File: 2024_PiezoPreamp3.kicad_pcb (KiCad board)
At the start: 4 copper layers, 71 x 36.8 mm, 90 parts, among them J101 6.3mm stereo, J102 6.3mm stereo, J201 DC IN 5.5/2.1mm, J401 Spring Contact, U101 OPA145, U102 OPA145, U201 ZXMP3A17E6TA, U301 BC847BS,115

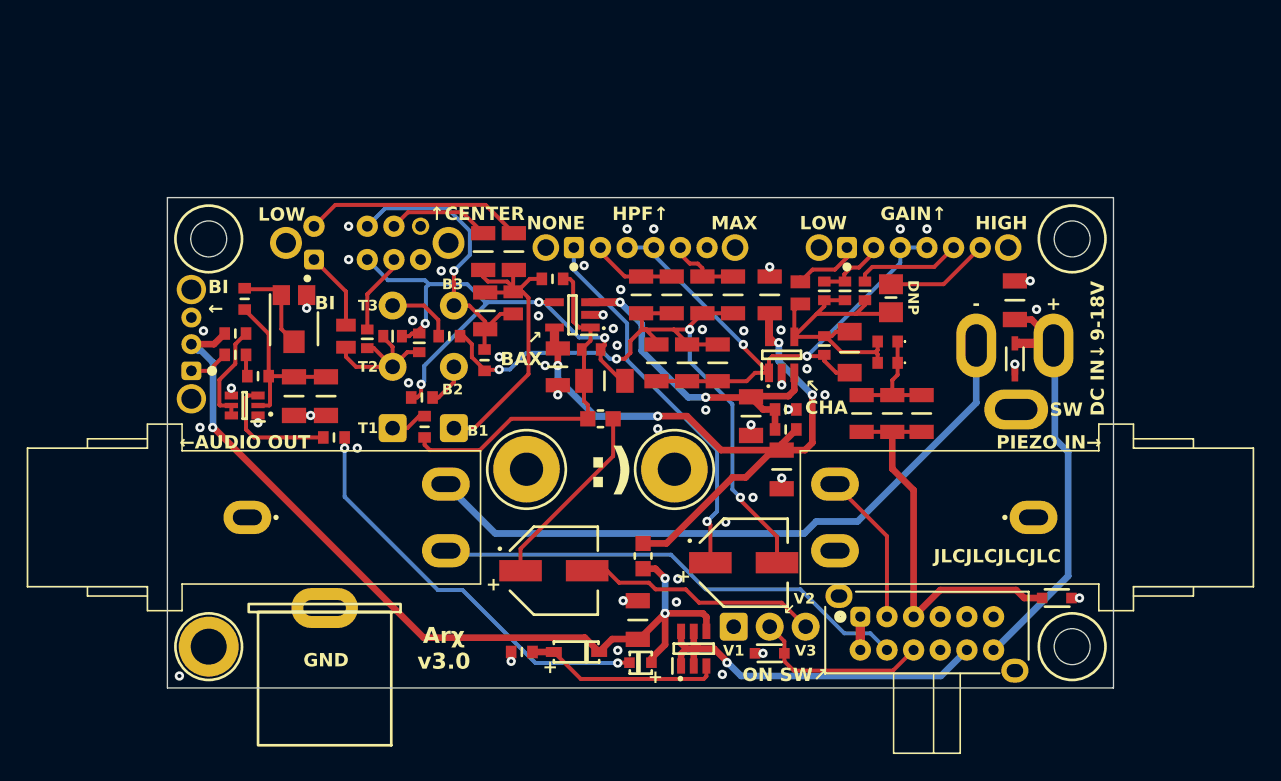
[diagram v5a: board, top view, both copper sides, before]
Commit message: PCB: moving tracks & vias so that the signals don't cross holes in gnd planes cause by signal vias
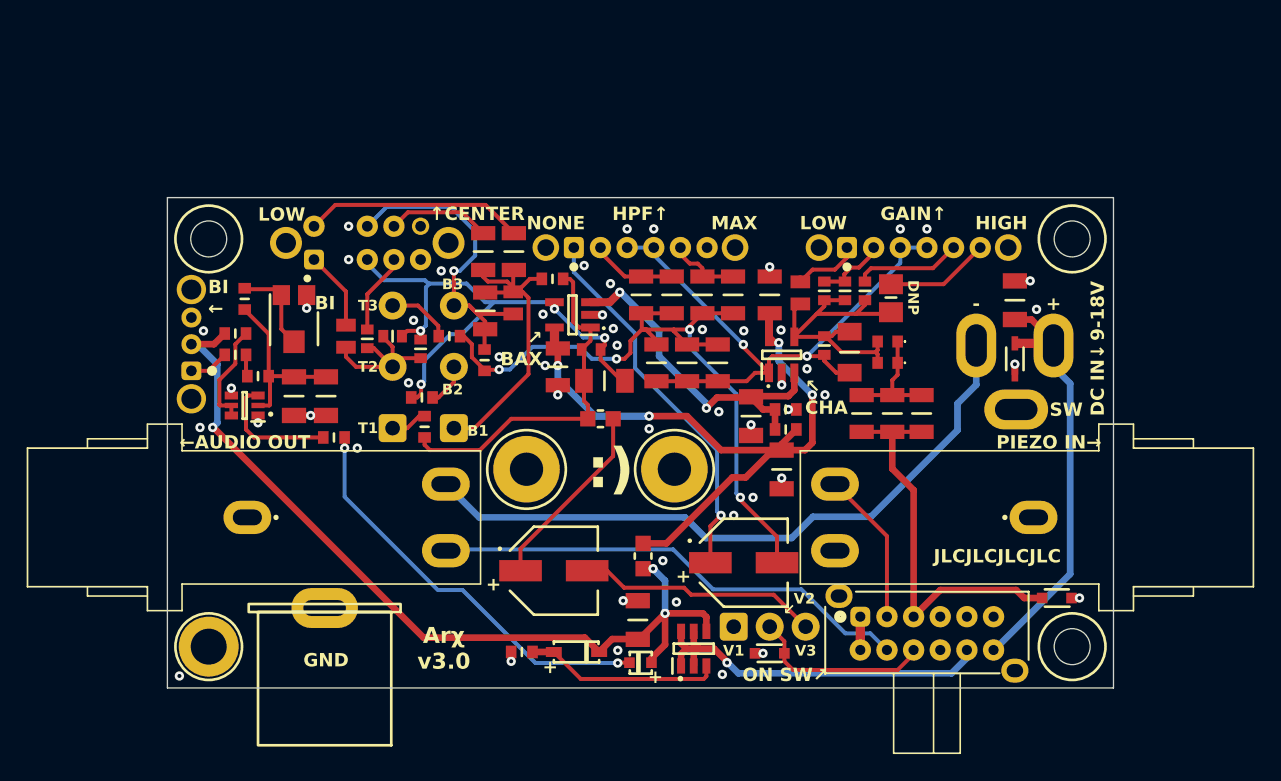
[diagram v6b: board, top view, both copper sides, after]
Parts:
- moved Ct101 0.46 mm to (133.9, 86.4)
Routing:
- net /1-ChargeAmpAndEQ/BASS_3: track 22.7 -> 24.5 mm
- net Vbias: track 24.7 -> 26.2 mm
- net DC_IN_NEG: track 49.7 -> 50.4 mm
- net VS: track 56.3 -> 55.7 mm
- net /1-ChargeAmpAndEQ/BAX_A_INV: track 41.0 -> 41.6 mm

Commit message: PCB: stitching vias
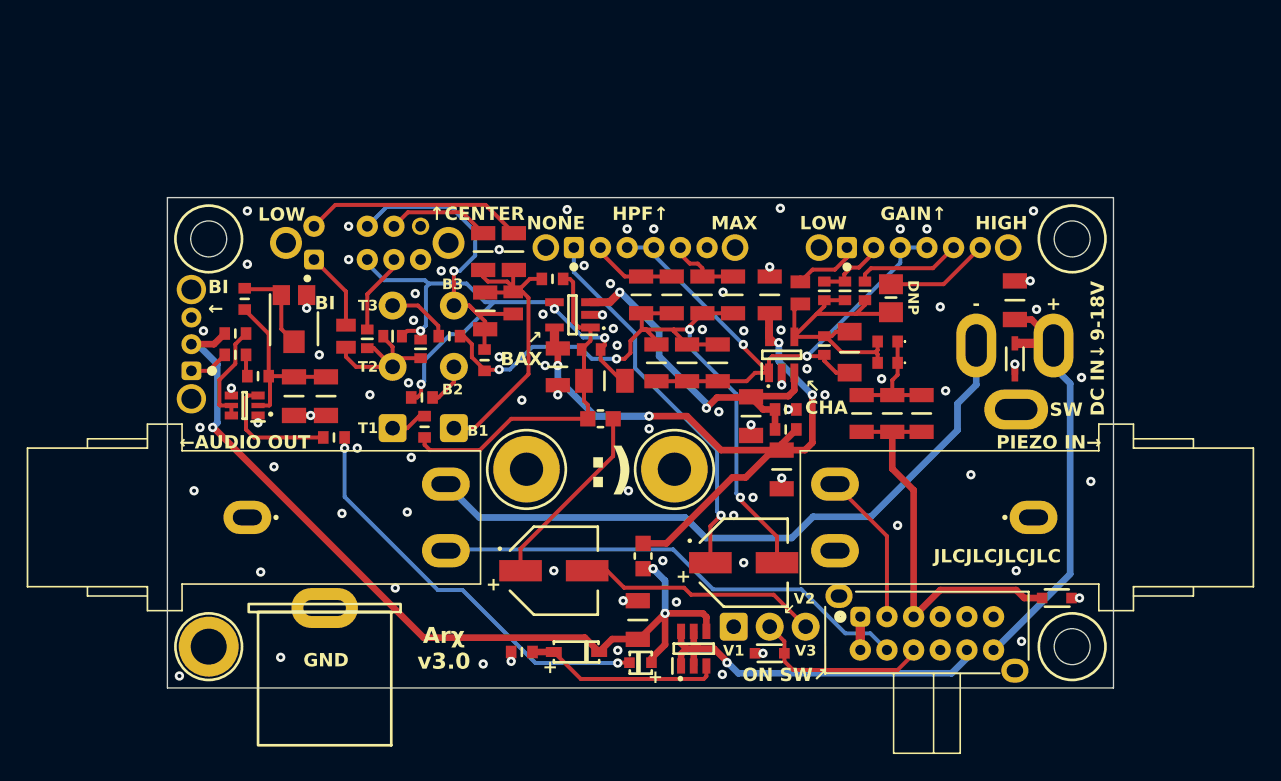
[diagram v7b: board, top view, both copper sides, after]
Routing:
- net GND: vias 51 -> 83
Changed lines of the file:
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@@
+	)
+	(via
+		(at 156.6 82.15)
+		(size 0.7)
+		(drill 0.3)
+		(layers "F.Cu" "B.Cu")
+		(net 2)
 	)
 	(via
@@
 	)
 	(via
+		(at 120.9 76.05)
+		(size 0.7)
+		(drill 0.3)
+		(layers "F.Cu" "B.Cu")
+		(net 2)
+	)
+	(via
 		(at 132.996268 88.950841)
 		(size 0.7)
@@
 	)
 	(via
+		(at 172.9 83.25)
+		(size 0.7)
+		(drill 0.3)
+		(layers "F.Cu" "B.Cu")
+		(net 2)
+	)
+	(via
 		(at 151.05 92.400003)
 		(size 0.7)
@@
 	)
 	(via
+		(at 128 98.75)
+		(size 0.7)
+		(drill 0.3)
+		(layers "F.Cu" "B.Cu")
+		(net 2)
+	)
+	(via
 		(at 159.6 109.25)
 		(size 0.7)
@@
 	)
 	(via
+		(at 143.9 103.05)
+		(size 0.7)
+		(drill 0.3)
+		(layers "F.Cu" "B.Cu")
+		(net 2)
+	)
+	(via
 		(at 152.083934 102.296651)
 		(size 0.7)
@@
 	)
 	(via
+		(at 175.2 95.85)
+		(size 0.7)
+		(drill 0.3)
+		(layers "F.Cu" "B.Cu")
+		(net 2)
+	)
+	(via
 		(at 161 89.1)
 		(size 0.7)
@@
 	)
 	(via
+		(at 133.2 94.55)
+		(size 0.7)
+		(drill 0.3)
+		(layers "F.Cu" "B.Cu")
+		(net 2)
+	)
+	(via
 		(at 148.151935 81.505632)
 		(size 0.7)
@@
 	)
 	(via
+		(at 169.7 99.65)
+		(size 0.7)
+		(drill 0.3)
+		(layers "F.Cu" "B.Cu")
+		(net 2)
+	)
+	(via
+		(at 158.15 102.45)
+		(size 0.7)
+		(drill 0.3)
+		(layers "F.Cu" "B.Cu")
+		(net 2)
+	)
+	(via
 		(at 135.449997 80.55)
 		(size 0.7)
@@
 	)
 	(via
+		(at 123.4 109.55)
+		(size 0.7)
+		(drill 0.3)
+		(layers "F.Cu" "B.Cu")
+		(net 2)
+	)
+	(via
 		(at 125.35 83.35)
 		(size 0.7)
@@
 	)
 	(via
+		(at 132 104.35)
+		(size 0.7)
+		(drill 0.3)
+		(layers "F.Cu" "B.Cu")
+		(net 2)
+	)
+	(via
 		(at 151.4 77.399997)
 		(size 0.7)
@@
 	)
 	(via
+		(at 168.5 88.65)
+		(size 0.7)
+		(drill 0.3)
+		(layers "F.Cu" "B.Cu")
+		(net 2)
+	)
+	(via
 		(at 153.1 105.4)
 		(size 0.7)
@@
 	)
 	(via
+		(at 132.9 98.65)
+		(size 0.7)
+		(drill 0.3)
+		(layers "F.Cu" "B.Cu")
+		(net 2)
+	)
+	(via
+		(at 144.9 75.95)
+		(size 0.7)
+		(drill 0.3)
+		(layers "F.Cu" "B.Cu")
+		(net 2)
+	)
+	(via
 		(at 149.1 105.3)
 		(size 0.7)
@@
 	)
 	(via
+		(at 120.9 80.05)
+		(size 0.7)
+		(drill 0.3)
+		(layers "F.Cu" "B.Cu")
+		(net 2)
+	)
+	(via
+		(at 121.9 103.15)
+		(size 0.7)
+		(drill 0.3)
+		(layers "F.Cu" "B.Cu")
+		(net 2)
+	)
+	(via
 		(at 119.7 89.35)
 		(size 0.7)
@@
 	)
 	(via
+		(at 133.5 82.25)
+		(size 0.7)
+		(drill 0.3)
+		(layers "F.Cu" "B.Cu")
+		(net 2)
+	)
+	(via
 		(at 156.284324 91.117758)
 		(size 0.7)
@@
 	)
 	(via
+		(at 184.2 96.35)
+		(size 0.7)
+		(drill 0.3)
+		(layers "F.Cu" "B.Cu")
+		(net 2)
+	)
+	(via
 		(at 121.7 91.95)
 		(size 0.7)
@@
 	)
 	(via
+		(at 179.9 76.05)
+		(size 0.7)
+		(drill 0.3)
+		(layers "F.Cu" "B.Cu")
+		(net 2)
+	)
+	(via
 		(at 178.5 87.55)
 		(size 0.7)
@@
 	)
 	(via
+		(at 138.6 110.05)
+		(size 0.7)
+		(drill 0.3)
+		(layers "F.Cu" "B.Cu")
+		(net 2)
+	)
+	(via
+		(at 139.8 78.95)
+		(size 0.7)
+		(drill 0.3)
+		(layers "F.Cu" "B.Cu")
+		(net 2)
+	)
+	(via
 		(at 171.9 77.399997)
 		(size 0.7)
@@
 	)
 	(via
+		(at 122.9 95.25)
+		(size 0.7)
+		(drill 0.3)
+		(layers "F.Cu" "B.Cu")
+		(net 2)
+	)
+	(via
+		(at 141.5 90.25)
+		(size 0.7)
+		(drill 0.3)
+		(layers "F.Cu" "B.Cu")
+		(net 2)
+	)
+	(via
+		(at 130.1 89.85)
+		(size 0.7)
+		(drill 0.3)
+		(layers "F.Cu" "B.Cu")
+		(net 2)
+	)
+	(via
+		(at 173.3 89.55)
+		(size 0.7)
+		(drill 0.3)
+		(layers "F.Cu" "B.Cu")
+		(net 2)
+	)
+	(via
 		(at 146.175095 80.146816)
 		(size 0.7)
@@
 	)
 	(via
+		(at 160.9 75.85)
+		(size 0.7)
+		(drill 0.3)
+		(layers "F.Cu" "B.Cu")
+		(net 2)
+	)
+	(via
+		(at 149.5 97.05)
+		(size 0.7)
+		(drill 0.3)
+		(layers "F.Cu" "B.Cu")
+		(net 2)
+	)
+	(via
 		(at 183.35 105.1)
 		(size 0.7)
@@
 	)
 	(via
+		(at 179 108.35)
+		(size 0.7)
+		(drill 0.3)
+		(layers "F.Cu" "B.Cu")
+		(net 2)
+	)
+	(via
 		(at 129.150003 93.85)
 		(size 0.7)
@@
 	)
 	(via
+		(at 178.6 103.05)
+		(size 0.7)
+		(drill 0.3)
+		(layers "F.Cu" "B.Cu")
+		(net 2)
+	)
+	(via
+		(at 183.5 88.55)
+		(size 0.7)
+		(drill 0.3)
+		(layers "F.Cu" "B.Cu")
+		(net 2)
+	)
+	(via
 		(at 143.089124 83.801742)
 		(size 0.7)
@@
 		(size 0.7)
 		(drill 0.3)
+		(layers "F.Cu" "B.Cu")
+		(net 2)
+	)
+	(via
+		(at 116.9 97.05)
+		(size 0.7)
+		(drill 0.3)
+		(layers "F.Cu" "B.Cu")
+		(net 2)
+	)
+	(via
+		(at 126.3 86.85)
+		(size 0.7)
+		(drill 0.3)

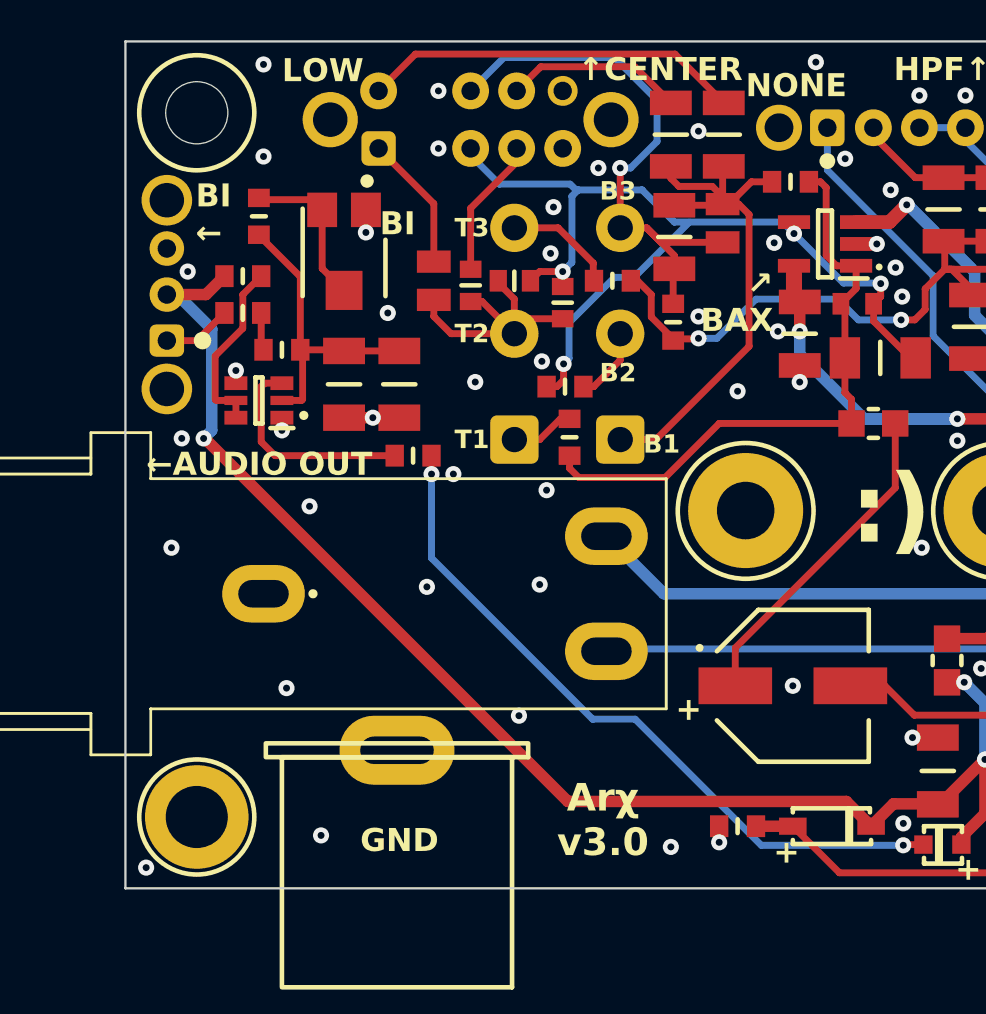
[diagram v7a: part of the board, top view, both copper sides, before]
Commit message: PCB: improving track aesthetics, some vias, zone corners. Setting plot outputs closer to JLC recommendation
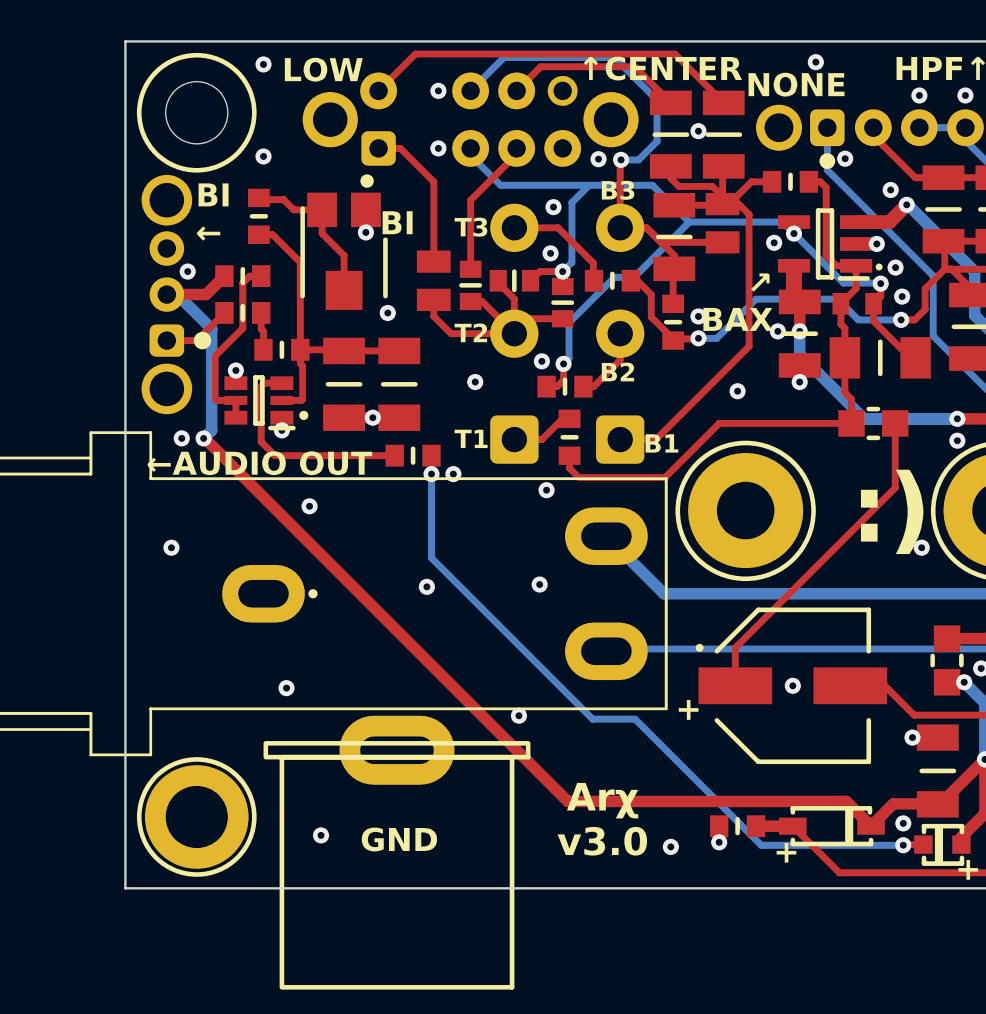
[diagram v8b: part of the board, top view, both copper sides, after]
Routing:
- net /1-ChargeAmpAndEQ/C_SW_1: track 5.91 -> 6.47 mm
- net GND: vias 83 -> 82
